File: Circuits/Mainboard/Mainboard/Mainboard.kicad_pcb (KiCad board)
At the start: 2 copper layers, 170 x 170 mm, 43 parts, among them IC1 LM74500QDDFRQ1, IC2 LM74500QDDFRQ1, IC3 2536030320001, IC4 SX1280IMLTRT, IC5 SKY66122-11, IC6 TS2596CM533_RNG, IC7 LM2576-5.0WU-TR, J1 XT60PW-M, J15 SMA-J-P-H-RA-TH1, J2 XT60PW-M, J4 Conn_01x05_Pin, Q1 PSMN6R7-40MLDX, Q2 PSMN6R7-40MLDX, U1 NUCLEOH723ZG

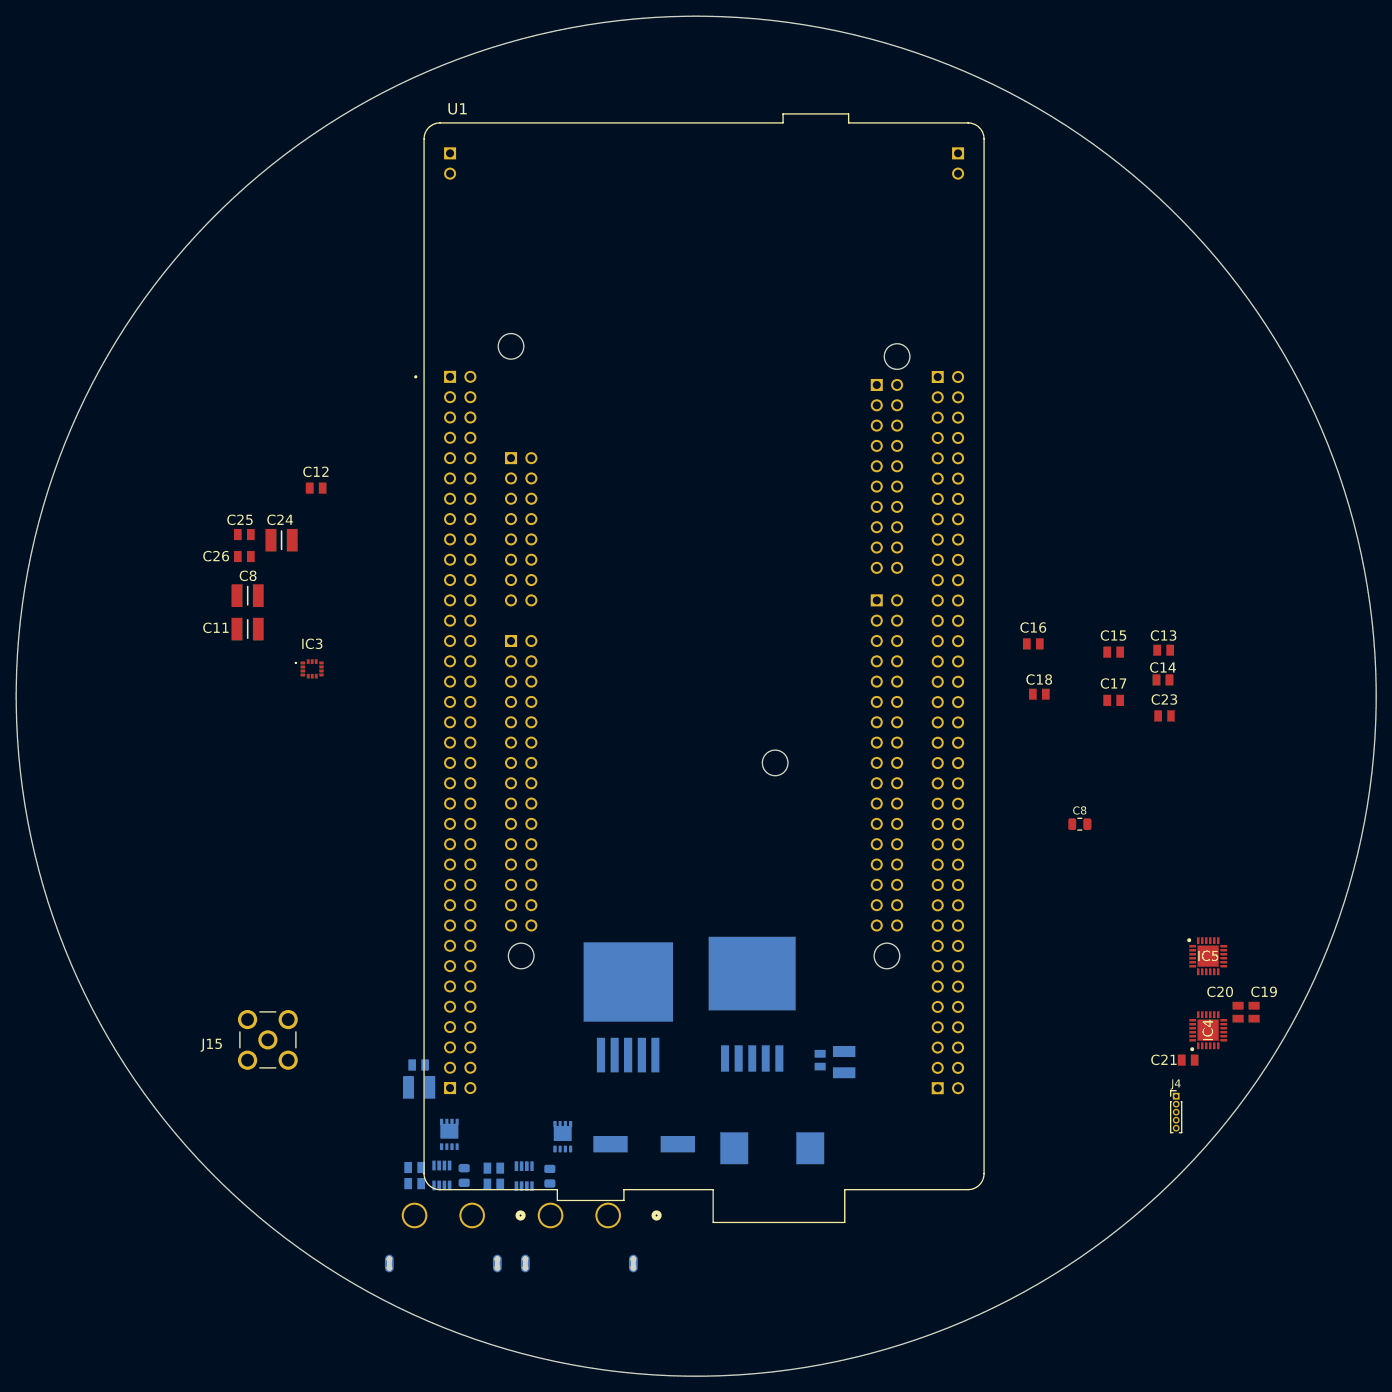
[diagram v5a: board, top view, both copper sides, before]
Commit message: Completet motor driver adapter board, added components for 3d rendering
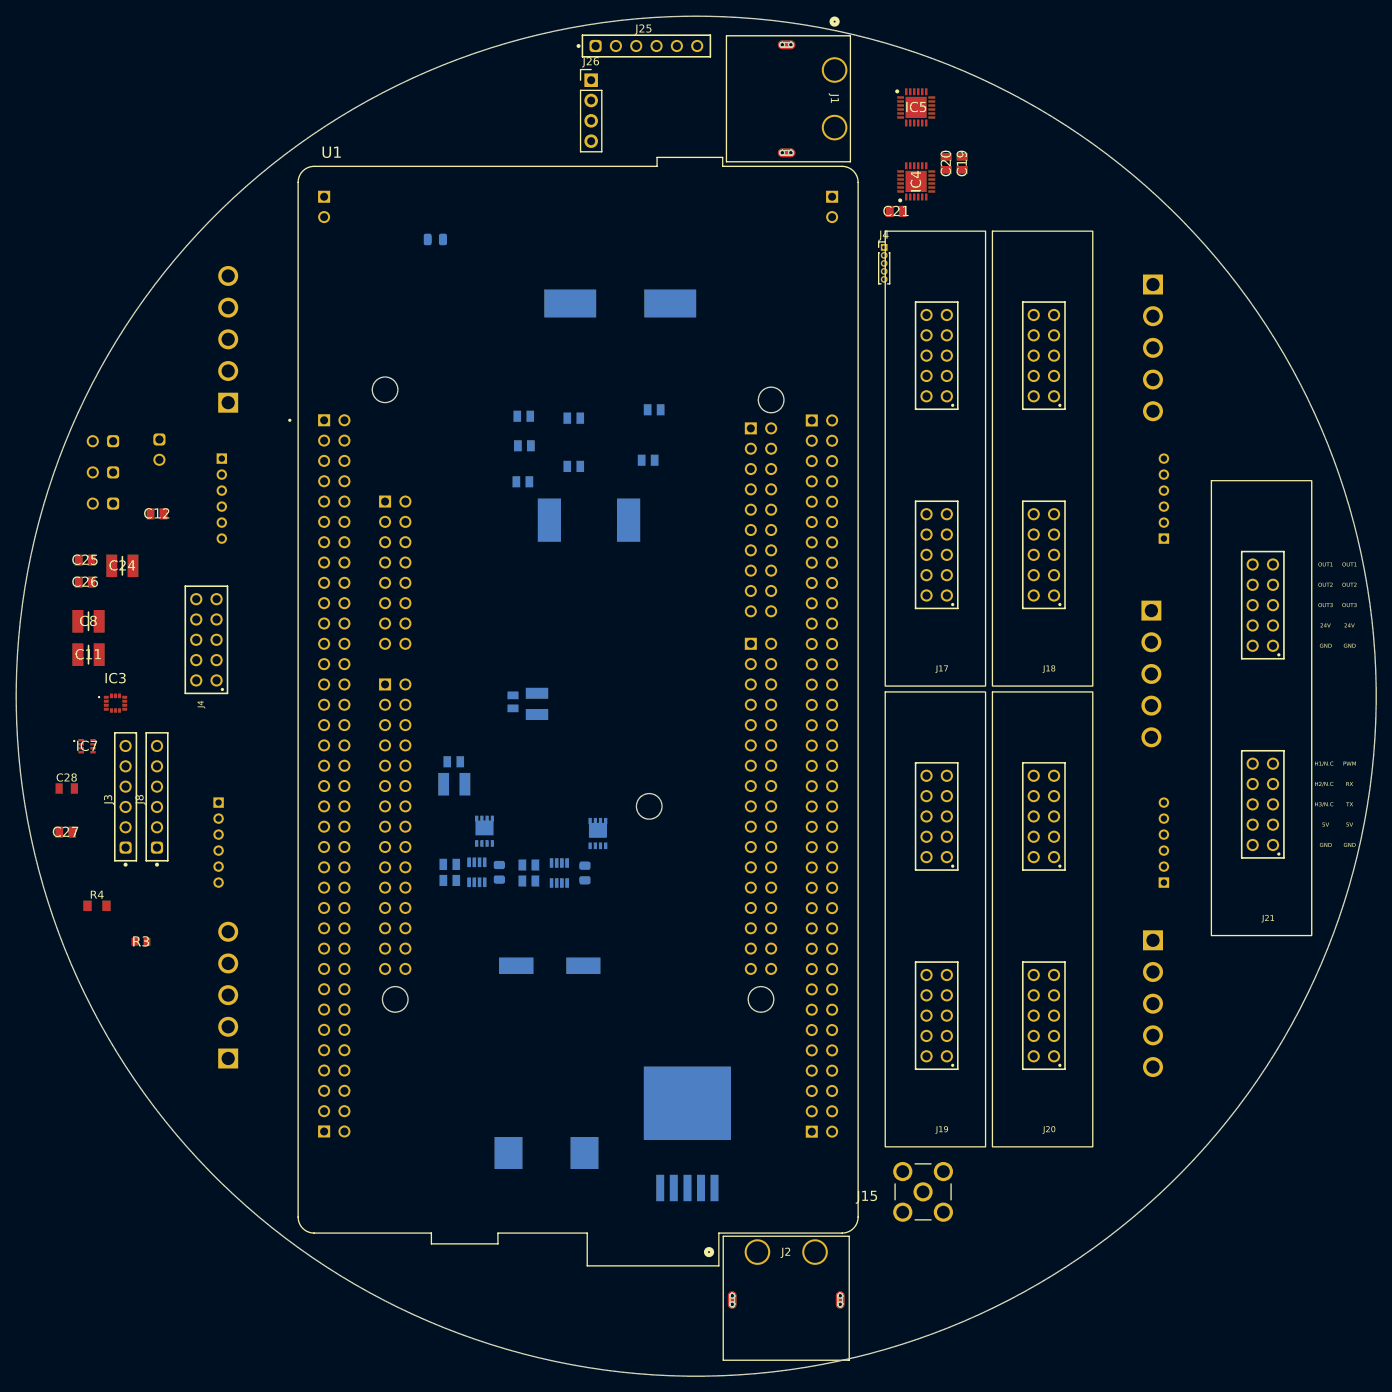
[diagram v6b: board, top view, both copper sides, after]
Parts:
- added C22: 470uF, Altium_WCAP-ASLL (rev24b):WCAP-ASLL_D16H17, B.Cu at (177.0, 79.4)
- added C27: 0.1uF, 885012007063:CAPC2012X90N, F.Cu at (107.7, 145.5)
- added C28: 47uF, Altium_WCAP-CSGP (rev24b):WCAP-CSGP_0805_L2W1.25H1.25, F.Cu at (107.8, 140.1)
- added J10: B5P-VH_LF__SN_, B5P-VH-LF-SN:B5P-VH_LF__SN_, B.Cu at (243.6, 77.0)
- added J11: B6B-PH-K-S, B6B-PH-K-S:JST_B6B-PH-K-S, B.Cu at (127.3, 146.8)
- added J12: B5P-VH_LF__SN_, B5P-VH-LF-SN:B5P-VH_LF__SN_, B.Cu at (128.0, 173.8)
- added J13: B6B-PH-K-S, B6B-PH-K-S:JST_B6B-PH-K-S, B.Cu at (244.4, 146.8)
- added J14: B5P-VH_LF__SN_, B5P-VH-LF-SN:B5P-VH_LF__SN_, B.Cu at (243.6, 159.0)
- added J16: B5P-VH_LF__SN_, B5P-VH-LF-SN:B5P-VH_LF__SN_, B.Cu at (243.4, 117.8)
- added J17: ~, 61301021821:ESC_Adapter_socket, F.Cu at (216.6, 117.9)
- added J18: ~, 61301021821:ESC_Adapter_socket, F.Cu at (230.0, 117.9)
- added J19: ~, 61301021821:ESC_Adapter_socket, F.Cu at (216.6, 175.5)
- added J20: ~, 61301021821:ESC_Adapter_socket, F.Cu at (230.0, 175.5)
- added J21: ~, 61301021821:ESC_Adapter_socket, F.Cu at (257.4, 149.1)
- added J22: 61300211821, Socket_header_6_pins_single_straight:61300211821, B.Cu at (112.3, 96.6)
- added J23: 61300211821, Socket_header_6_pins_single_straight:61300211821, B.Cu at (112.3, 100.5)
- added J24: 61300211821, Socket_header_6_pins_single_straight:61300211821, B.Cu at (112.3, 104.4)
- added J25: Conn_01x06_Pin, Socket_header_6_pins_single_straight:61300611821, F.Cu at (180.3, 47.2)
- added J26: Conn_01x04_Pin, Connector_PinHeader_2.54mm:PinHeader_1x04_P2.54mm_Vertical, F.Cu at (173.4, 51.5)
- added J3: Conn_01x06_Pin, Socket_header_6_pins_single_straight:61300611821, F.Cu at (115.2, 141.1)
- added J4: ~, 61301021821:61301021821, F.Cu at (125.3, 121.5)
- added J5: B6B-PH-K-S, B6B-PH-K-S:JST_B6B-PH-K-S, B.Cu at (127.8, 103.8)
- added J6: B5P-VH_LF__SN_, B5P-VH-LF-SN:B5P-VH_LF__SN_, B.Cu at (128.0, 91.8)
- added J7: B6B-PH-K-S, B6B-PH-K-S:JST_B6B-PH-K-S, B.Cu at (244.4, 103.8)
- added J8: Conn_01x06_Pin, Socket_header_6_pins_single_straight:61300611821, F.Cu at (119.1, 141.1)
- added J9: 61300211821, Socket_header_6_pins_single_straight:61300211821, B.Cu at (119.4, 97.7)
- added L1: 8.2uH, WE-HCC (rev24a):WE-HCC_1210, B.Cu at (173.1, 106.5)
- added R3: 52.3kOhm, CRCW060352K3FKEA:RESC1608X50N, F.Cu at (117.1, 159.2)
- added R4: 10kOhm, Altium_WRIS-RSKS (rev23a):WRIS-RSKS_0805_Wave, F.Cu at (111.6, 154.7)
- C13, C14, C15, C16, C17, C18, C23, C8: moved to B.Cu
- IC7: value LM2576-5.0WU-TR -> TPS563300DRLR; footprint LM2576-5.0WU-TR:5-PIN-TO-263_U_ -> TPS563300DRLR:TPS62932DRLR; moved to F.Cu
- J1, J2: moved to F.Cu
- moved J1 146.0 mm to (203.8, 50.2), turned to -90 degrees
- moved C19 112.2 mm to (219.8, 61.9)
- moved C20 112.2 mm to (217.8, 61.9)
- moved C21 112.2 mm to (211.5, 67.9)
- moved IC4 112.2 mm to (214.0, 64.2)
- moved IC5 112.2 mm to (214.0, 54.9)
- moved J4 112.2 mm to (210.0, 72.4)
- moved C8 108.8 mm to (153.9, 71.4), turned to 180 degrees
- moved C23 85.4 mm to (164.8, 101.7), turned to 180 degrees
- moved C13 85.2 mm to (164.9, 93.5), turned to 180 degrees
- moved C14 85.0 mm to (165.0, 97.2), turned to 180 degrees
- moved J15 84.1 mm to (214.9, 190.5)
- moved C15 73.6 mm to (171.2, 93.7), turned to 180 degrees
- moved C17 73.6 mm to (171.2, 99.8), turned to 180 degrees
- moved IC7 72.7 mm to (110.4, 134.8), turned to 0 degrees
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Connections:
- IC7 pad 1: 24V -> unconnected-(IC7-NC_1-Pad1)
- IC7 pad 3: GND -> 24V
- IC7 pad 4: unconnected-(IC7-FEEDBACK-Pad4) -> GND
- IC7 pad 5: GND -> Net-(IC7-SW)
- IC7 pad 6: unconnected-(IC7-TAB-Pad6) -> Net-(IC7-BST)
- U1 pad CN11_2: unconnected-(U1A-PC11-PadCN11_2) -> /M5_RX
- U1 pad CN11_21: /BNO055_SDA -> /SEN0374_SDA
- U1 pad CN11_28: unconnected-(U1A-PA0-PadCN11_28) -> /M5_TX
- U1 pad CN11_3: unconnected-(U1A-PC12-PadCN11_3) -> /Rpi_TX
- U1 pad CN11_46: unconnected-(U1A-PE2-PadCN11_46) -> /M4_RX
- U1 pad CN11_47: unconnected-(U1A-PE3-PadCN11_47) -> /M4_TX
- U1 pad CN11_51: /VL53L1_SCL -> /VL53L4CD_SCL
- U1 pad CN11_53: /VL53L1_SDA -> /VL53L4CD_SDA
- U1 pad CN12_16: unconnected-(U1B-PB12-PadCN12_16) -> /Rpi_RX
- U1 pad CN12_17: unconnected-(U1B-PB6-PadCN12_17) -> /M1_TX
- U1 pad CN12_19: unconnected-(U1B-PC7-PadCN12_19) -> /M3_RX
- U1 pad CN12_26: unconnected-(U1B-PB15-PadCN12_26) -> /M1_RX
- U1 pad CN12_3: /BNO055_SCL -> /SEN0374_SCL
- U1 pad CN12_35: unconnected-(U1B-PA2-PadCN12_35) -> /M2_TX
- U1 pad CN12_37: unconnected-(U1B-PA3-PadCN12_37) -> /M2_RX
- U1 pad CN12_4: unconnected-(U1B-PC6-PadCN12_4) -> /M3_TX
- U1 pad CN12_50: unconnected-(U1B-PF14-PadCN12_50) -> /ADPS-9960_SCL
- U1 pad CN12_60: unconnected-(U1B-PF15-PadCN12_60) -> /ADPS-9960_SDA
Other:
- board text added: "24V"
- board text added: "5V"
- board text added: "GND"
- board text added: "H1/N.C"
- board text added: "H2/N.C"
- board text added: "H3/N.C"
- board text added: "OUT1"
- board text added: "OUT2"
- board text added: "OUT3"
- board text added: "PWM"
- board text added: "RX"
- board text added: "TX"

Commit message: Step file for the mainboard pcb
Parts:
- J1, J2: footprint XT60PW-M:CONN_XT60PW-M_AMA -> Connector_AMASS:AMASS_XT60PW-M_1x02_P7.20mm_Horizontal; moved to B.Cu
- moved J1 155.7 mm to (190.6, 205.4), turned to 90 degrees
- moved J26 84.4 mm to (132.6, 125.4)
- moved C8 68.9 mm to (222.5, 65.7)
- moved J4 22.5 mm to (227.4, 58.1)
- moved J2 10.2 mm to (183.9, 198.3), turned to -90 degrees
- moved C15 7.62 mm to (164.9, 98.0)
- moved L1 7.62 mm to (166.8, 110.8)
- moved C17 7.62 mm to (164.9, 104.0)
- moved C22 7.49 mm to (169.7, 77.9)
- moved U1 7.17 mm to (174.7, 122.4)
- moved C13 6.40 mm to (169.7, 97.8)
- moved C14 6.40 mm to (169.8, 101.5)
- moved C16 6.40 mm to (186.0, 97.0)
- moved C18 6.40 mm to (185.2, 103.3)
- moved C23 6.40 mm to (169.6, 106.0)
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
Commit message: Step file for mainboard pcb updated layout
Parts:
- removed J24: 61300211821, Socket_header_6_pins_single_straight:61300211821
- removed the J4 at (227.4, 58.1)
- added J27: Conn_01x04_Pin, Connector_PinHeader_2.54mm:PinHeader_1x04_P2.54mm_Vertical, B.Cu at (264.5, 146.6)
- C11, C12, C24, C25, C26, C27, C28, C8, IC3, IC7, R3, R4: moved to B.Cu
- C15, C16, C17, C18, J16: moved to F.Cu
- J22, J23, J9: value 61300211821 -> Conn_01x04_Pin; footprint Socket_header_6_pins_single_straight:61300211821 -> Connector_PinHeader_2.54mm:PinHeader_1x04_P2.54mm_Vertical
- moved J9 144.9 mm to (264.2, 101.5), turned to 180 degrees
- moved J1 142.9 mm to (206.7, 63.4), turned to -90 degrees
- moved J25 129.9 mm to (119.5, 162.0), turned to -90 degrees
- moved J16 125.8 mm to (122.0, 84.8)
- moved IC5 119.6 mm to (228.7, 173.6)
- moved C20 107.4 mm to (224.8, 169.1)
- moved C19 106.4 mm to (232.4, 167.6), turned to -90 degrees
- moved IC4 104.8 mm to (228.7, 167.9)
- moved C21 97.1 mm to (224.1, 164.2)
- moved C11 88.1 mm to (168.4, 189.8), turned to 180 degrees
- moved C15 87.4 mm to (228.6, 157.8)
- moved C17 86.0 mm to (228.6, 161.8)
- moved C27 83.1 mm to (186.3, 118.3), turned to 180 degrees
- moved C28 82.9 mm to (186.1, 112.8), turned to 180 degrees
- moved R4 77.7 mm to (176.1, 111.5), turned to 180 degrees
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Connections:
- J11 pad 2: /5V_RF -> /5V
- J22 pad 1: /M2_Encoder_A -> /5V
- J22 pad 2: /M2_Encoder_B -> /M1_Encoder_A
- J23 pad 1: /M1_Encoder_A -> /5V
- J23 pad 2: /M1_Encoder_B -> /M3_Encoder_A
- J9 pad 1: /M4_Encoder_A -> /5V
- J9 pad 2: /M4_Encoder_B -> /M2_Encoder_A
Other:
- board size 170 x 170 mm -> 170.1 x 170.1 mm
- board text added: "2.8V"
- board text added: "3.3V"
- board text added: "ADPS-9960_INT"
- board text added: "ADPS-9960_SCL"
- board text added: "ADPS-9960_SDA"
- board text added: "ADPS-9960_VL"
- board text added: "Dribbler"
- board text added: "M1_H1"
- board text added: "M1_H2"
- board text added: "M1_H3"
- board text added: "M2_CH_A"
- board text added: "M2_CH_B"
- board text added: "M2_H1"
- board text added: "M2_H2"
- board text added: "M2_H3"
- board text added: "M3_H1"
- board text added: "M3_H2"
- board text added: "M3_H3"
- board text added: "M4_CH_A"
- board text added: "M4_CH_B"
- board text added: "M4_H1"
- board text added: "M4_H2"
- board text added: "M4_H3"
- board text added: "M5_OUT1"
- board text added: "M5_OUT2"
- board text added: "M5_OUT3"
- board text added: "Raspberry Pi"
- board text added: "Rpi_RX"
- board text added: "Rpi_TX"
- board text added: "SEN0374_BL-IND"
- board text added: "SEN0374_Boot"
- board text added: "SEN0374_INT"
- board text added: "SEN0374_PS1"
- board text added: "SEN0374_PS2"
- board text added: "SEN0374_RST"
- board text added: "SEN0374_SCL"
- board text added: "SEN0374_SDA"
- board text added: "VL53L4CD_INT"
- board text added: "VL53L4CD_SCL"
- board text added: "VL53L4CD_SDA"
- board text added: "VL53L4CD_SHUT"
- board text added: "VL6180_IO0"
- board text added: "VL6180_IO1"
- board text added: "VL6180_SCL"
- board text added: "VL6180_SDA"
